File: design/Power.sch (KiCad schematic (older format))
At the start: 49 parts, among them U2 NCP1117ST33T3G, U3 DRV8302

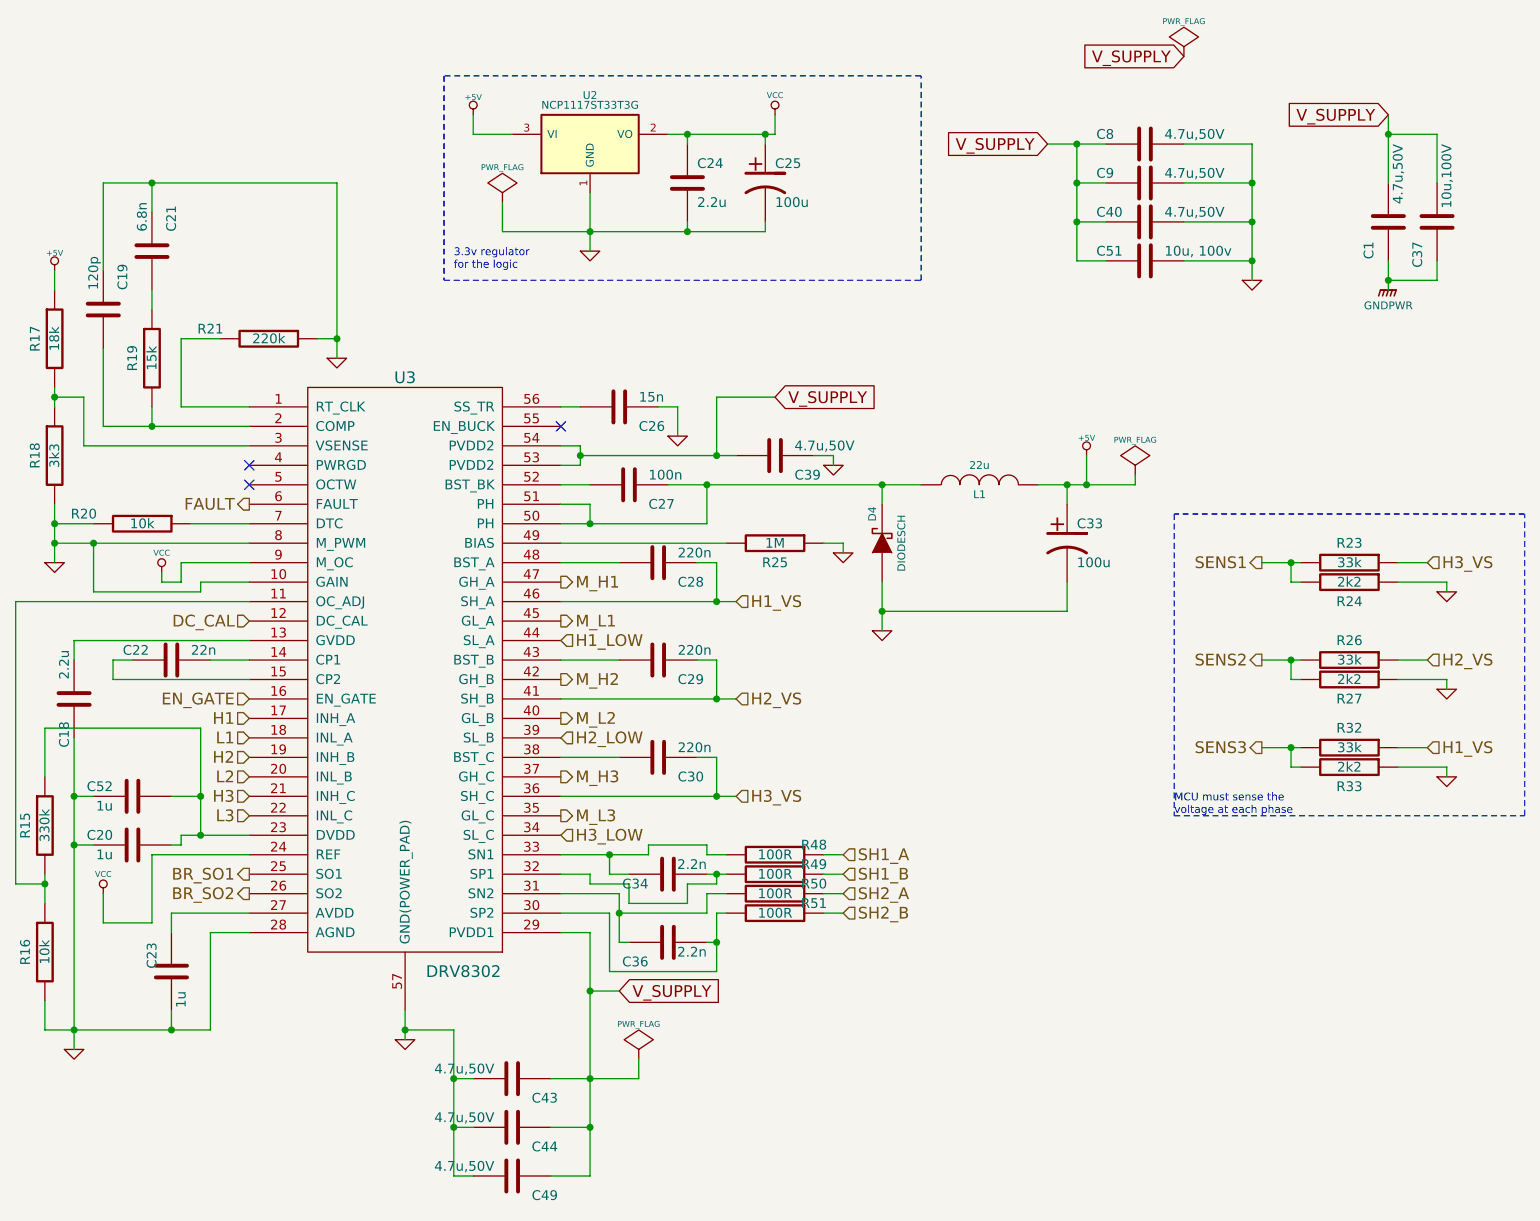
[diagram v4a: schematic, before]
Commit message: Updated schematic from previous commit
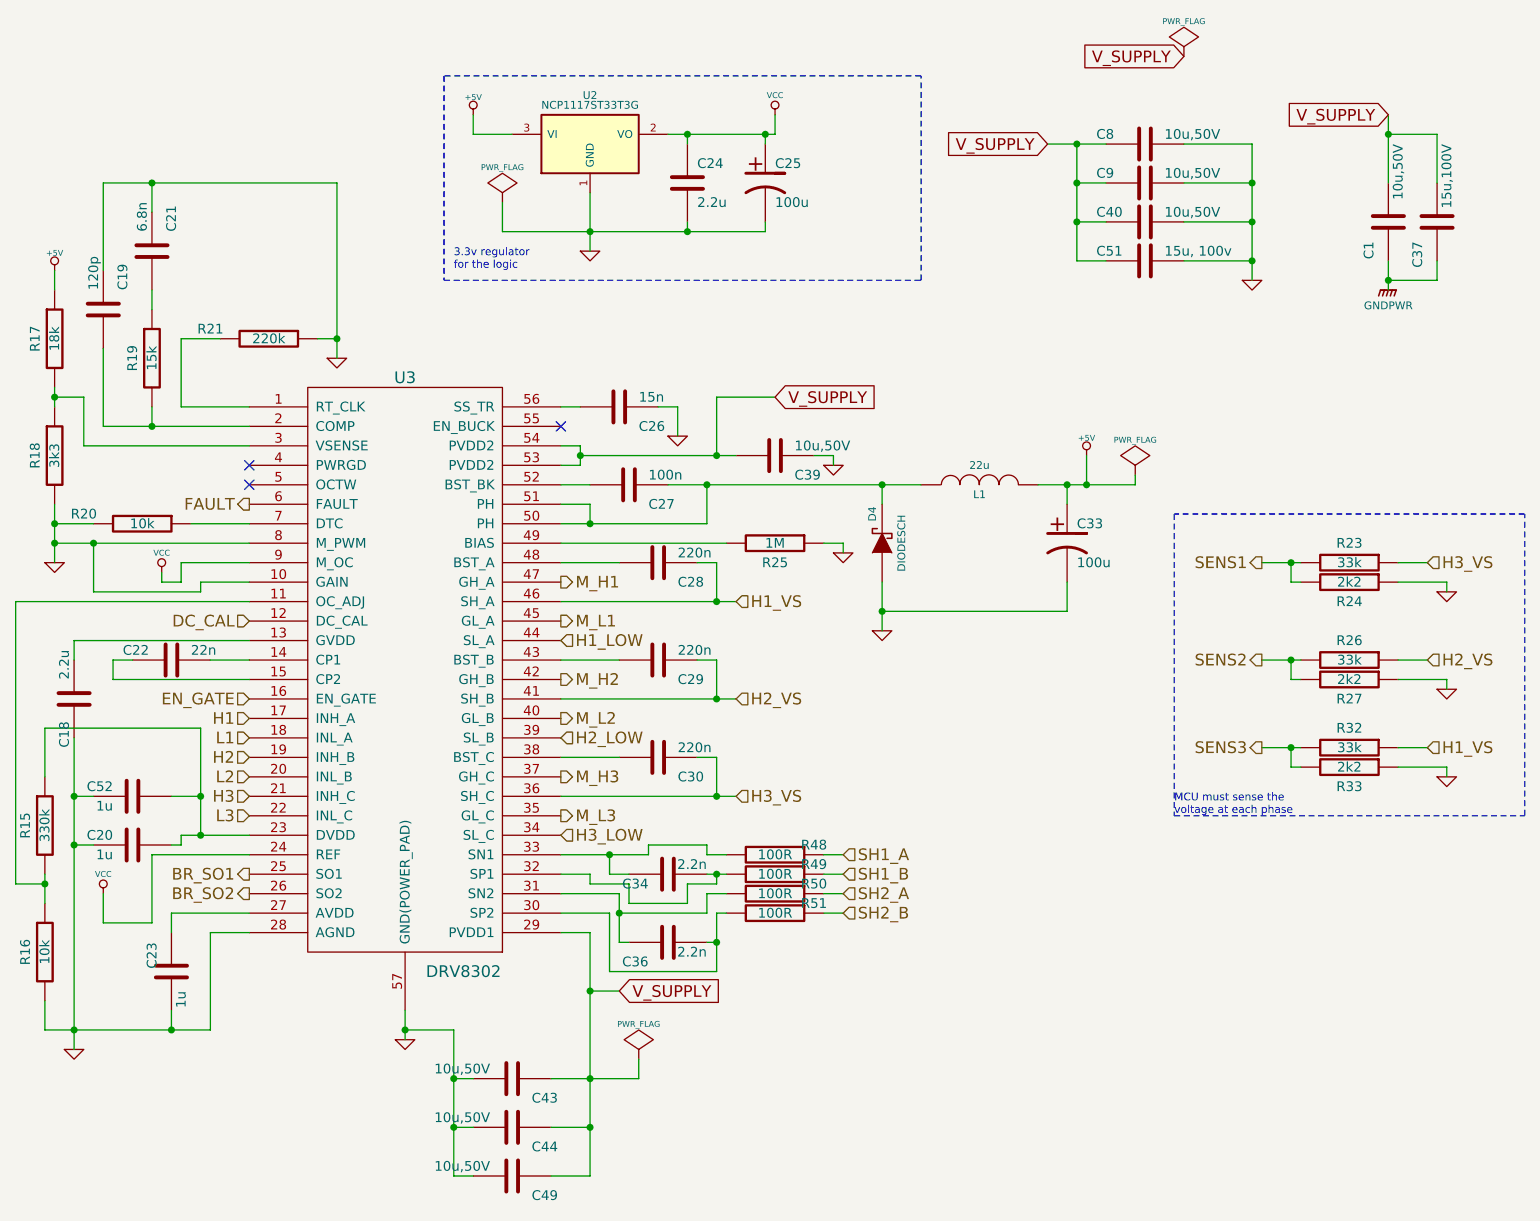
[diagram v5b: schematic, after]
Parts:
- C1, C39, C40, C43, C44, C49, C8, C9: value 4.7u,50V -> 10u,50V
- C37: value 10u,100V -> 15u,100V
- C51: value 10u, 100v -> 15u, 100v
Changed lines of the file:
@@
 $EndComp
 $Comp
-L GND #PWR050
+L GND #PWR051
 U 1 1 504F8F7B
 P 10700 3500
-F 0 "#PWR050" H 10700 3500 30  0001 C CNN
+F 0 "#PWR051" H 10700 3500 30  0001 C CNN
 F 1 "GND" H 10700 3430 30  0001 C CNN
 F 2 "" H 10700 3500 60  0001 C CNN
@@
 $EndComp
 $Comp
-L GND #PWR051
+L GND #PWR052
 U 1 1 504F8F8D
 P 10700 4000
-F 0 "#PWR051" H 10700 4000 30  0001 C CNN
+F 0 "#PWR052" H 10700 4000 30  0001 C CNN
 F 1 "GND" H 10700 3930 30  0001 C CNN
 F 2 "" H 10700 4000 60  0001 C CNN
@@
 $EndComp
 $Comp
-L GND #PWR052
+L GND #PWR053
 U 1 1 504F8FAF
 P 10700 4450
-F 0 "#PWR052" H 10700 4450 30  0001 C CNN
+F 0 "#PWR053" H 10700 4450 30  0001 C CNN
 F 1 "GND" H 10700 4380 30  0001 C CNN
 F 2 "" H 10700 4450 60  0001 C CNN
@@
 $EndComp
 $Comp
-L GND #PWR053
+L GND #PWR054
 U 1 1 504FB755
 P 6750 2700
-F 0 "#PWR053" H 6750 2700 30  0001 C CNN
+F 0 "#PWR054" H 6750 2700 30  0001 C CNN
 F 1 "GND" H 6750 2630 30  0001 C CNN
 F 2 "" H 6750 2700 60  0001 C CNN
@@
 $EndComp
 $Comp
-L GND #PWR054
+L GND #PWR055
 U 1 1 504FBA7B
 P 7600 3300
-F 0 "#PWR054" H 7600 3300 30  0001 C CNN
+F 0 "#PWR055" H 7600 3300 30  0001 C CNN
 F 1 "GND" H 7600 3230 30  0001 C CNN
 F 2 "" H 7600 3300 60  0001 C CNN
@@
 $EndComp
 $Comp
-L GND #PWR055
+L GND #PWR056
 U 1 1 504FBEC1
 P 7800 3700
-F 0 "#PWR055" H 7800 3700 30  0001 C CNN
+F 0 "#PWR056" H 7800 3700 30  0001 C CNN
 F 1 "GND" H 7800 3630 30  0001 C CNN
 F 2 "" H 7800 3700 60  0001 C CNN
@@
 $EndComp
 $Comp
-L +5V #PWR056
+L +5V #PWR057
 U 1 1 504FBFA1
 P 8850 2800
-F 0 "#PWR056" H 8850 2890 20  0001 C CNN
+F 0 "#PWR057" H 8850 2890 20  0001 C CNN
 F 1 "+5V" H 8850 2890 30  0000 C CNN
 F 2 "" H 8850 2800 60  0001 C CNN
@@
 $EndComp
 $Comp
-L GND #PWR057
+L GND #PWR058
 U 1 1 504FC2A8
 P 3650 5850
-F 0 "#PWR057" H 3650 5850 30  0001 C CNN
+F 0 "#PWR058" H 3650 5850 30  0001 C CNN
 F 1 "GND" H 3650 5780 30  0001 C CNN
 F 2 "" H 3650 5850 60  0001 C CNN
@@
 $EndComp
 $Comp
-L GND #PWR058
+L GND #PWR059
 U 1 1 504FC918
 P 5350 5800
-F 0 "#PWR058" H 5350 5800 30  0001 C CNN
+F 0 "#PWR059" H 5350 5800 30  0001 C CNN
 F 1 "GND" H 5350 5730 30  0001 C CNN
 F 2 "" H 5350 5800 60  0001 C CNN
@@
 $EndComp
 $Comp
-L GND #PWR059
+L GND #PWR060
 U 1 1 504FDE04
 P 3550 3350
-F 0 "#PWR059" H 3550 3350 30  0001 C CNN
+F 0 "#PWR060" H 3550 3350 30  0001 C CNN
 F 1 "GND" H 3550 3280 30  0001 C CNN
 F 2 "" H 3550 3350 60  0001 C CNN
@@
 $EndComp
 $Comp
-L GND #PWR060
+L GND #PWR061
 U 1 1 504FE598
 P 5000 2300
-F 0 "#PWR060" H 5000 2300 30  0001 C CNN
+F 0 "#PWR061" H 5000 2300 30  0001 C CNN
 F 1 "GND" H 5000 2230 30  0001 C CNN
 F 2 "" H 5000 2300 60  0001 C CNN
@@
 $EndComp
 $Comp
-L +5V #PWR061
+L +5V #PWR062
 U 1 1 504FE8CD
 P 3550 1850
-F 0 "#PWR061" H 3550 1940 20  0001 C CNN
+F 0 "#PWR062" H 3550 1940 20  0001 C CNN
 F 1 "+5V" H 3550 1940 30  0000 C CNN
 F 2 "" H 3550 1850 60  0001 C CNN
@@
 $EndComp
 $Comp
-L GND #PWR062
+L GND #PWR063
 U 1 1 50500B40
 P 6300 1750
-F 0 "#PWR062" H 6300 1750 30  0001 C CNN
+F 0 "#PWR063" H 6300 1750 30  0001 C CNN
 F 1 "GND" H 6300 1680 30  0001 C CNN
 F 2 "" H 6300 1750 60  0001 C CNN
@@
 $EndComp
 $Comp
-L VCC #PWR063
+L VCC #PWR064
 U 1 1 50500B46
 P 7250 1050
-F 0 "#PWR063" H 7250 1150 30  0001 C CNN
+F 0 "#PWR064" H 7250 1150 30  0001 C CNN
 F 1 "VCC" H 7250 1150 30  0000 C CNN
 F 2 "" H 7250 1050 60  0001 C CNN
@@
 $EndComp
 $Comp
-L +5V #PWR064
+L +5V #PWR065
 U 1 1 50500BBC
 P 5700 1050
-F 0 "#PWR064" H 5700 1140 20  0001 C CNN
+F 0 "#PWR065" H 5700 1140 20  0001 C CNN
 F 1 "+5V" H 5700 1140 30  0000 C CNN
 F 2 "" H 5700 1050 60  0001 C CNN
@@
 $EndComp
 $Comp
-L VCC #PWR065
+L VCC #PWR066
 U 1 1 505014BC
 P 3800 5050
-F 0 "#PWR065" H 3800 5150 30  0001 C CNN
+F 0 "#PWR066" H 3800 5150 30  0001 C CNN
 F 1 "VCC" H 3800 5150 30  0000 C CNN
 F 2 "" H 3800 5050 60  0001 C CNN
@@
 $EndComp
 $Comp
-L PWR_FLAG #FLG066
+L PWR_FLAG #FLG067
 U 1 1 50510100
 P 9100 2900
-F 0 "#FLG066" H 9100 2995 30  0001 C CNN
+F 0 "#FLG067" H 9100 2995 30  0001 C CNN
 F 1 "PWR_FLAG" H 9100 3080 30  0000 C CNN
 F 2 "" H 9100 2900 60  0001 C CNN
@@
 $EndComp
 $Comp
-L PWR_FLAG #FLG067
+L PWR_FLAG #FLG068
 U 1 1 505104A0
 P 5850 1500
-F 0 "#FLG067" H 5850 1595 30  0001 C CNN
+F 0 "#FLG068" H 5850 1595 30  0001 C CNN
 F 1 "PWR_FLAG" H 5850 1680 30  0000 C CNN
 F 2 "" H 5850 1500 60  0001 C CNN
@@
 $EndComp
 $Comp
-L PWR_FLAG #FLG068
+L PWR_FLAG #FLG069
 U 1 1 505105A5
 P 9350 750
-F 0 "#FLG068" H 9350 845 30  0001 C CNN
+F 0 "#FLG069" H 9350 845 30  0001 C CNN
 F 1 "PWR_FLAG" H 9350 930 30  0000 C CNN
 F 2 "" H 9350 750 60  0001 C CNN
@@
 $EndComp
 $Comp
-L GND #PWR069
+L GND #PWR070
 U 1 1 5051337C
 P 7550 2850
-F 0 "#PWR069" H 7550 2850 30  0001 C CNN
+F 0 "#PWR070" H 7550 2850 30  0001 C CNN
 F 1 "GND" H 7550 2780 30  0001 C CNN
 F 2 "" H 7550 2850 60  0001 C CNN
@@
 $EndComp
 $Comp
-L VCC #PWR070
+L VCC #PWR071
 U 1 1 5058357A
 P 4100 3400
-F 0 "#PWR070" H 4100 3500 30  0001 C CNN
+F 0 "#PWR071" H 4100 3500 30  0001 C CNN
 F 1 "VCC" H 4100 3500 30  0000 C CNN
 F 2 "" H 4100 3400 60  0001 C CNN
@@
 P 7250 2800
 F 0 "C39" V 7350 2900 50  0000 L CNN
-F 1 "4.7u,50V" V 7200 2900 50  0000 L CNN
+F 1 "10u,50V" V 7200 2900 50  0000 L CNN
 F 2 "SMD_Packages:SMD-1206" H 7250 2800 60  0001 C CNN
 F 3 "" H 7250 2800 60  0001 C CNN
@@
 P 5900 6000
 F 0 "C43" V 6000 6100 50  0000 L CNN
-F 1 "4.7u,50V" V 5850 5600 50  0000 L CNN
+F 1 "10u,50V" V 5850 5600 50  0000 L CNN
 F 2 "SMD_Packages:SMD-1206" H 5900 6000 60  0001 C CNN
 F 3 "" H 5900 6000 60  0001 C CNN
@@
 P 5900 6250
 F 0 "C44" V 6000 6350 50  0000 L CNN
-F 1 "4.7u,50V" V 5850 5850 50  0000 L CNN
+F 1 "10u,50V" V 5850 5850 50  0000 L CNN
 F 2 "SMD_Packages:SMD-1206" H 5900 6250 60  0001 C CNN
 F 3 "" H 5900 6250 60  0001 C CNN
@@
 V_SUPPLY
 $Comp
-L PWR_FLAG #FLG071
+L PWR_FLAG #FLG072
 U 1 1 50C62060
 P 6550 5900
-F 0 "#FLG071" H 6550 5995 30  0001 C CNN
+F 0 "#FLG072" H 6550 5995 30  0001 C CNN
 F 1 "PWR_FLAG" H 6550 6080 30  0000 C CNN
 F 2 "" H 6550 5900 60  0001 C CNN
@@
 P 5900 6500
 F 0 "C49" V 6000 6600 50  0000 L CNN
-F 1 "4.7u,50V" V 5850 6100 50  0000 L CNN
+F 1 "10u,50V" V 5850 6100 50  0000 L CNN
 F 2 "SMD_Packages:SMD-1206" H 5900 6500 60  0001 C CNN
 F 3 "" H 5900 6500 60  0001 C CNN
@@
 P 9150 1800
 F 0 "C51" V 9100 1550 50  0000 L CNN
-F 1 "10u, 100v" V 9100 1900 50  0000 L CNN
+F 1 "15u, 100v" V 9100 1900 50  0000 L CNN
 F 2 "w_smd_cap:c_2220" H 9150 1800 60  0001 C CNN
 F 3 "" H 9150 1800 60  0001 C CNN
@@
 $EndComp
 $Comp
-L GND #PWR072
+L GND #PWR073
 U 1 1 510944D0
 P 9700 1900
-F 0 "#PWR072" H 9700 1900 30  0001 C CNN
+F 0 "#PWR073" H 9700 1900 30  0001 C CNN
 F 1 "GND" H 9700 1830 30  0001 C CNN
 F 2 "" H 9700 1900 60  0001 C CNN
@@
 P 10400 1600
 F 0 "C1" V 10500 1700 50  0000 L CNN
-F 1 "4.7u,50V" V 10350 1200 50  0000 L CNN
+F 1 "10u,50V" V 10350 1200 50  0000 L CNN
 F 2 "SMD_Packages:SMD-1206" H 10400 1600 60  0001 C CNN
 F 3 "" H 10400 1600 60  0001 C CNN
@@
 P 10650 1600
 F 0 "C37" V 10750 1700 50  0000 L CNN
-F 1 "10u,100V" V 10600 1200 50  0000 L CNN
+F 1 "15u,100V" V 10600 1200 50  0000 L CNN
 F 2 "w_smd_cap:c_2220" H 10650 1600 60  0001 C CNN
 F 3 "" H 10650 1600 60  0001 C CNN
@@
 P 9150 1600
 F 0 "C40" V 9100 1350 50  0000 L CNN
-F 1 "4.7u,50V" V 9100 1700 50  0000 L CNN
+F 1 "10u,50V" V 9100 1700 50  0000 L CNN
 F 2 "SMD_Packages:SMD-1206" H 9150 1600 60  0001 C CNN
 F 3 "" H 9150 1600 60  0001 C CNN
@@
 P 9150 1400
 F 0 "C9" V 9100 1150 50  0000 L CNN
-F 1 "4.7u,50V" V 9100 1500 50  0000 L CNN
+F 1 "10u,50V" V 9100 1500 50  0000 L CNN
 F 2 "SMD_Packages:SMD-1206" H 9150 1400 60  0001 C CNN
 F 3 "" H 9150 1400 60  0001 C CNN
@@
 P 9150 1200
 F 0 "C8" V 9100 950 50  0000 L CNN
-F 1 "4.7u,50V" V 9100 1300 50  0000 L CNN
+F 1 "10u,50V" V 9100 1300 50  0000 L CNN
 F 2 "SMD_Packages:SMD-1206" H 9150 1200 60  0001 C CNN
 F 3 "" H 9150 1200 60  0001 C CNN
@@
 00 FD 87 A8 17 00 00 00 00 F4 1F A2 5E 00 00 00 00 D0 7F 88 7A 01 00 00 00 40 FF 21 EA 05 00 00
 00 00 FD 87 A8 17 00 00 00 00 F4 1F A2 5E 00 00 00 00 D0 7F 88 7A 01 00 00 00 40 FF 21 EA 05 00
-00 00 00 FD F7 3F 90 37 91 24 49 74 FD E2 00 00 00 00 49 45 4E 44 AE 42 60 82 20
+00 00 00 FD F7 3F 90 37 91 24 49 74 FD E2 00 00 00 00 49 45 4E 44 AE 42 60 82 00
 EndData
 $EndBitmap
@@
 SH2_B
 $Comp
-L GNDPWR #PWR073
+L GNDPWR #PWR074
 U 1 1 53FA36C6
 P 10400 1950
-F 0 "#PWR073" H 10400 2000 40  0001 C CNN
+F 0 "#PWR074" H 10400 2000 40  0001 C CNN
 F 1 "GNDPWR" H 10400 1870 40  0000 C CNN
 F 2 "" H 10400 1950 60  0000 C CNN
@@
 	4550 5250 4350 5250
 Wire Wire Line
-	4350 5750 4350 5250
+	4350 5250 4350 5750
 Wire Wire Line
-	3500 5750 4350 5750
+	4350 5750 3500 5750
 Wire Wire Line
 	4150 5750 4150 5650
@@
 0D 0D 85 50 5B 08 A1 71 E3 C6 45 47 47 77 AB F8 CD C0 F0 65 C3 18 9A 0F 4F 4B 4B 4B 51 51 51 53
 53 93 40 20 30 31 31 61 94 40 19 18 18 43 C3 C0 C0 A0 72 FE 07 CF 64 8C 61 E1 12 74 DD 00 00 00
-00 49 45 4E 44 AE 42 60 82 4F
+00 49 45 4E 44 AE 42 60 82 01
 EndData
 $EndBitmap
@@
 20 10 88 31 C3 77 F3 62 81 40 20 10 08 04 02 81 E0 1F 14 E4 21 10 08 04 02 81 40 8C 41 50 90 87
 40 20 10 08 04 02 31 06 41 41 1E 02 81 40 20 10 08 C4 18 E4 FF 01 14 B1 03 90 4A B9 68 69 00 00
-00 00 49 45 4E 44 AE 42 60 82 20
+00 00 49 45 4E 44 AE 42 60 82 00
 EndData
 $EndBitmap
@@
 A1 C7 18 00 00 C0 28 C8 B2 00 00 00 46 41 96 05 00 00 30 0A B2 2C 00 00 80 51 90 65 01 00 00 8C
 82 2C 0B 00 00 60 14 64 59 00 00 00 A3 FC 7F BD 9B 69 A6 C1 67 F0 EA 00 00 00 00 49 45 4E 44 AE
-42 60 82 DD
+42 60 82 18
 EndData
 $EndBitmap
@@
 AB D8 39 0B 59 91 9E DF A8 2A 5B EE 54 3A FD 71 ED 71 2F 29 C3 82 EC 80 87 06 6E C3 98 10 30 3B
 62 9A BB 2D 03 B8 C4 64 FC B5 26 AC 13 9B D1 39 40 41 C1 D6 78 4C 84 BF 94 F0 6F E1 BF 96 F0 0F
-FF 77 E2 FF 1F 0F 43 55 32 21 1C 08 16 00 00 00 00 49 45 4E 44 AE 42 60 82 43
+FF 77 E2 FF 1F 0F 43 55 32 21 1C 08 16 00 00 00 00 49 45 4E 44 AE 42 60 82 32
 EndData
 $EndBitmap

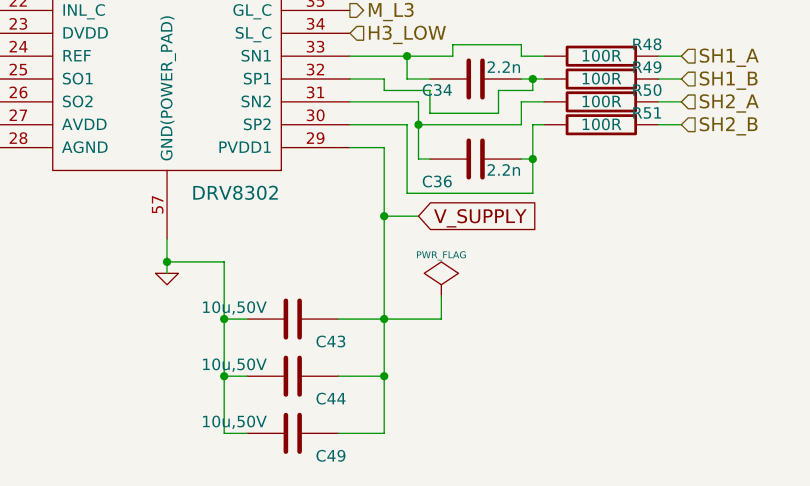
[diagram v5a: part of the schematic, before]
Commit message: Moved nRST cap closer to the MCU pin, connected crystal GND pins to the actual GND plane. Added several vias to GND and VDD planes.
Signed-off-by: Marcos Chaparro <marcos@mrkindustries.com.ar>
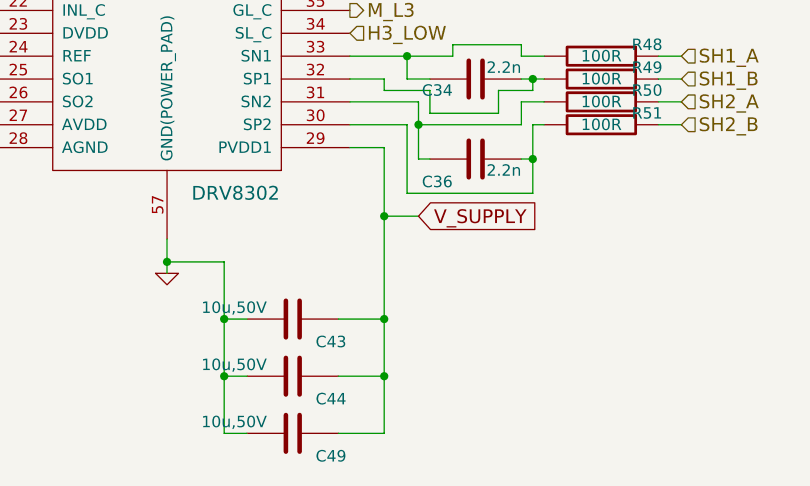
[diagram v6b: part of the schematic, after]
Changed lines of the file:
@@
 V_SUPPLY
 $Comp
-L PWR_FLAG #FLG072
-U 1 1 50C62060
-P 6550 5900
-F 0 "#FLG072" H 6550 5995 30  0001 C CNN
-F 1 "PWR_FLAG" H 6550 6080 30  0000 C CNN
-F 2 "" H 6550 5900 60  0001 C CNN
-F 3 "" H 6550 5900 60  0001 C CNN
-	1    6550 5900
-	1    0    0    -1
-$EndComp
-$Comp
 L C C49
 U 1 1 51093C64
@@
 $EndComp
 $Comp
-L GND #PWR073
+L GND #PWR072
 U 1 1 510944D0
 P 9700 1900
-F 0 "#PWR073" H 9700 1900 30  0001 C CNN
+F 0 "#PWR072" H 9700 1900 30  0001 C CNN
 F 1 "GND" H 9700 1830 30  0001 C CNN
 F 2 "" H 9700 1900 60  0001 C CNN
@@
 $Bitmap
 Pos 4700 7150
-Scale 0,000000
+Scale 0.000000
 Data
 89 50 4E 47 0D 0A 1A 0A 00 00 00 0D 49 48 44 52 00 00 03 A7 00 00 01 FE 08 02 00 00 00 EF 60 EF
@@
 SH2_B
 $Comp
-L GNDPWR #PWR074
+L GNDPWR #PWR073
 U 1 1 53FA36C6
 P 10400 1950
-F 0 "#PWR074" H 10400 2000 40  0001 C CNN
+F 0 "#PWR073" H 10400 2000 40  0001 C CNN
 F 1 "GNDPWR" H 10400 1870 40  0000 C CNN
 F 2 "" H 10400 1950 60  0000 C CNN
@@
 	5600 5750 5600 6500
 Wire Wire Line
-	6100 6000 6550 6000
+	6100 6000 6300 6000
 Wire Wire Line
 	5600 6250 5700 6250
@@
 	6300 6250 6100 6250
 Connection ~ 6300 6000
-Wire Wire Line
-	6550 6000 6550 5900
 Connection ~ 5600 6250
 Wire Wire Line
@@
 $Bitmap
 Pos 1800 2050
-Scale 2,000000
+Scale 2.000000
 Data
 89 50 4E 47 0D 0A 1A 0A 00 00 00 0D 49 48 44 52 00 00 01 78 00 00 01 6A 08 02 00 00 00 9F E1 D6
@@
 0D 0D 85 50 5B 08 A1 71 E3 C6 45 47 47 77 AB F8 CD C0 F0 65 C3 18 9A 0F 4F 4B 4B 4B 51 51 51 53
 53 93 40 20 30 31 31 61 94 40 19 18 18 43 C3 C0 C0 A0 72 FE 07 CF 64 8C 61 E1 12 74 DD 00 00 00
-00 49 45 4E 44 AE 42 60 82 01
+00 49 45 4E 44 AE 42 60 82 AD
 EndData
 $EndBitmap
 $Bitmap
 Pos 1900 7000
-Scale 1,000000
+Scale 1.000000
 Data
 89 50 4E 47 0D 0A 1A 0A 00 00 00 0D 49 48 44 52 00 00 03 4C 00 00 01 C7 08 02 00 00 00 03 17 4F
@@
 20 10 88 31 C3 77 F3 62 81 40 20 10 08 04 02 81 E0 1F 14 E4 21 10 08 04 02 81 40 8C 41 50 90 87
 40 20 10 08 04 02 31 06 41 41 1E 02 81 40 20 10 08 C4 18 E4 FF 01 14 B1 03 90 4A B9 68 69 00 00
-00 00 49 45 4E 44 AE 42 60 82 00
+00 00 49 45 4E 44 AE 42 60 82 01
 EndData
 $EndBitmap
 $Bitmap
 Pos 10100 5700
-Scale 1,000000
+Scale 1.000000
 Data
 89 50 4E 47 0D 0A 1A 0A 00 00 00 0D 49 48 44 52 00 00 02 77 00 00 01 E7 08 02 00 00 00 55 26 EC
@@
 A1 C7 18 00 00 C0 28 C8 B2 00 00 00 46 41 96 05 00 00 30 0A B2 2C 00 00 80 51 90 65 01 00 00 8C
 82 2C 0B 00 00 60 14 64 59 00 00 00 A3 FC 7F BD 9B 69 A6 C1 67 F0 EA 00 00 00 00 49 45 4E 44 AE
-42 60 82 18
+42 60 82 85
 EndData
 $EndBitmap
@@
 $Bitmap
 Pos 8000 6050
-Scale 0,000000
+Scale 0.000000
 Data
 89 50 4E 47 0D 0A 1A 0A 00 00 00 0D 49 48 44 52 00 00 02 80 00 00 02 80 08 02 00 00 00 83 AF 5E
@@
 AB D8 39 0B 59 91 9E DF A8 2A 5B EE 54 3A FD 71 ED 71 2F 29 C3 82 EC 80 87 06 6E C3 98 10 30 3B
 62 9A BB 2D 03 B8 C4 64 FC B5 26 AC 13 9B D1 39 40 41 C1 D6 78 4C 84 BF 94 F0 6F E1 BF 96 F0 0F
-FF 77 E2 FF 1F 0F 43 55 32 21 1C 08 16 00 00 00 00 49 45 4E 44 AE 42 60 82 32
+FF 77 E2 FF 1F 0F 43 55 32 21 1C 08 16 00 00 00 00 49 45 4E 44 AE 42 60 82 BD
 EndData
 $EndBitmap
